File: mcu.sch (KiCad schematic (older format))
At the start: 17 parts, among them J3 debug+programing, J4 I2c oled, U4 STM32F103C8Tx, U5 SM353LT

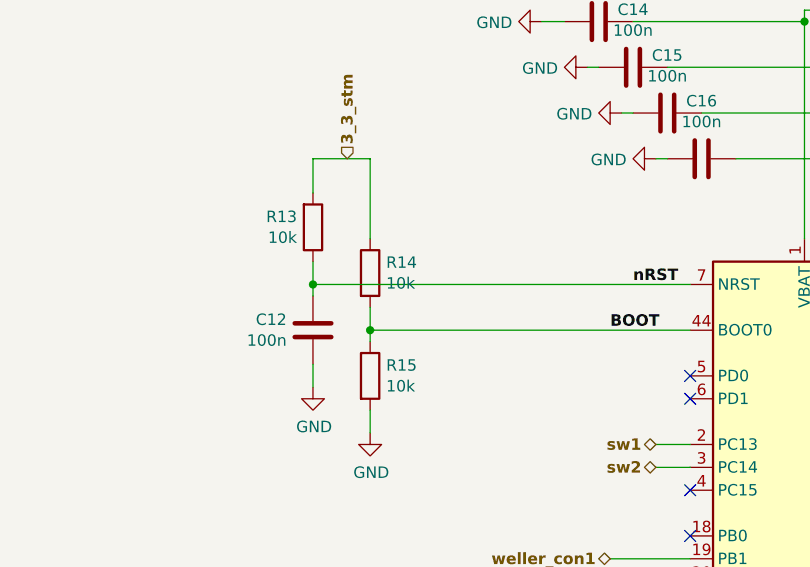
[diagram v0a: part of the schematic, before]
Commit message: update błędnego podpięcia pmosa na wejściu do układu, oras software testujący oled, przyciski i ledy
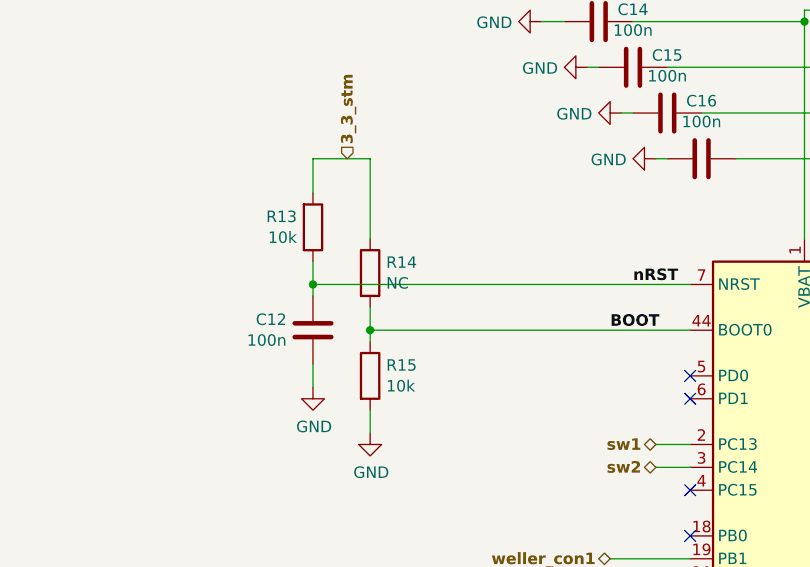
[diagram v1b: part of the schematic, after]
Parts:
- R14: value 10k -> NC
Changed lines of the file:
@@
 Wire Wire Line
 	6600 1200 6700 1200
-Text HLabel 4500 1850 1    50   Input ~ 6
+Text HLabel 4500 1850 1    50   Input ~ 10
 3_3_stm
-Text Label 6900 1600 0    50   ~ 6
+Text Label 6900 1600 0    50   ~ 10
 3_3v_analog
 $Comp
@@
 Wire Wire Line
 	4600 3050 4600 2950
-Text HLabel 6700 1050 1    50   Input ~ 6
+Text HLabel 6700 1050 1    50   Input ~ 10
 3_3_stm
 Wire Wire Line
@@
 Wire Wire Line
 	4350 1850 4350 2000
-Text HLabel 5850 3100 0    50   BiDi ~ 6
+Text HLabel 5850 3100 0    50   BiDi ~ 10
 sw1
-Text HLabel 5850 3200 0    50   BiDi ~ 6
+Text HLabel 5850 3200 0    50   BiDi ~ 10
 sw2
-Text HLabel 5750 3800 0    50   Output ~ 6
+Text HLabel 5750 3800 0    50   Output ~ 10
 led_g
-Text HLabel 5750 3900 0    50   Output ~ 6
+Text HLabel 5750 3900 0    50   Output ~ 10
 led_r
-Text HLabel 5750 4000 0    50   Output ~ 6
+Text HLabel 5750 4000 0    50   Output ~ 10
 led_y
-Text HLabel 5650 3600 0    50   BiDi ~ 6
+Text HLabel 5650 3600 0    50   BiDi ~ 10
 weller_con1
-Text HLabel 7650 4600 2    50   Output ~ 6
+Text HLabel 7650 4600 2    50   Output ~ 10
 PWM_heater
 Wire Wire Line
@@
 Wire Wire Line
 	7300 4900 7650 4900
-Text Label 7650 4800 0    50   ~ 6
+Text Label 7650 4800 0    50   ~ 10
 SWDIO
-Text Label 7650 4900 0    50   ~ 6
+Text Label 7650 4900 0    50   ~ 10
 SWCLK
-Text Label 5750 2400 0    50   ~ 6
+Text Label 5750 2400 0    50   ~ 10
 nRST
 Wire Wire Line
@@
 Wire Wire Line
 	6500 5500 6600 5500
-Text Label 1900 6850 0    50   ~ 6
+Text Label 1900 6850 0    50   ~ 10
 nRST
-Text Label 1900 6450 0    50   ~ 6
+Text Label 1900 6450 0    50   ~ 10
 SWDIO
-Text Label 1900 6550 0    50   ~ 6
+Text Label 1900 6550 0    50   ~ 10
 SWCLK
 Connection ~ 6900 1950
@@
 Wire Wire Line
 	6700 1650 6700 2200
-Text Label 5650 2600 0    50   ~ 6
+Text Label 5650 2600 0    50   ~ 10
 BOOT
 $Comp
@@
 Wire Wire Line
 	1550 3900 1100 3900
-Text HLabel 1100 3800 0    50   Input ~ 6
+Text HLabel 1100 3800 0    50   Input ~ 10
 3_3_stm
 Wire Wire Line
@@
 Wire Wire Line
 	1550 3600 1100 3600
-Text Label 1100 3600 0    50   ~ 6
+Text Label 1100 3600 0    50   ~ 10
 sda
-Text Label 1100 3700 0    50   ~ 6
+Text Label 1100 3700 0    50   ~ 10
 scl
-Text Label 5750 4200 0    50   ~ 6
+Text Label 5750 4200 0    50   ~ 10
 sda
 Wire Wire Line
 	5750 4200 6000 4200
-Text Label 5750 4100 0    50   ~ 6
+Text Label 5750 4100 0    50   ~ 10
 scl
 Wire Wire Line
@@
 Wire Wire Line
 	1300 3700 1100 3700
-Text HLabel 1150 3300 0    50   Input ~ 6
+Text HLabel 1150 3300 0    50   Input ~ 10
 3_3_stm
 Wire Wire Line
@@
 Wire Wire Line
 	7400 3800 7300 3800
-Text HLabel 7400 3800 2    50   Input ~ 6
+Text HLabel 7400 3800 2    50   Input ~ 10
 termocouple
 NoConn ~ 7300 3700
@@
 	-1   0    0    -1
 $EndComp
-Text Label 7650 3500 2    50   ~ 6
+Text Label 7650 3500 2    50   ~ 10
 hall_in
 Wire Wire Line
 	7300 3500 7650 3500
-Text Label 1150 5200 2    50   ~ 6
+Text Label 1150 5200 2    50   ~ 10
 hall_in
 $Comp
@@
 Wire Wire Line
 	1800 4900 1800 4850
-Text HLabel 1800 4800 1    50   Input ~ 6
+Text HLabel 1800 4800 1    50   Input ~ 10
 3_3_stm
 Wire Wire Line
 	1150 5200 1200 5200
-Text HLabel 1200 6450 0    50   Input ~ 6
+Text HLabel 1200 6450 0    50   Input ~ 10
 3_3_stm
 $Comp
@@
 Wire Wire Line
 	7300 4300 7650 4300
-Text Label 7650 4300 2    50   ~ 6
+Text Label 7650 4300 2    50   ~ 10
 usart_rx
-Text Label 7650 4400 2    50   ~ 6
+Text Label 7650 4400 2    50   ~ 10
 usart_tx
-Text Label 7650 4500 2    50   ~ 6
+Text Label 7650 4500 2    50   ~ 10
 usart_ck
 Wire Wire Line
@@
 Wire Wire Line
 	7300 4400 7650 4400
-Text Label 1200 6550 2    50   ~ 6
+Text Label 1200 6550 2    50   ~ 10
 usart_rx
-Text Label 1200 6650 2    50   ~ 6
+Text Label 1200 6650 2    50   ~ 10
 usart_tx
-Text Label 1200 6750 2    50   ~ 6
+Text Label 1200 6750 2    50   ~ 10
 usart_ck
 Wire Wire Line
@@
 Wire Wire Line
 	7400 3600 7300 3600
-Text HLabel 7400 3600 2    50   Input ~ 6
+Text HLabel 7400 3600 2    50   Input ~ 10
 input_sense
 NoConn ~ 7300 3900
@@
 P 4600 2350
 F 0 "R14" H 4670 2396 50  0000 L CNN
-F 1 "10k" H 4670 2305 50  0000 L CNN
+F 1 "NC" H 4670 2305 50  0000 L CNN
 F 2 "Resistor_SMD:R_0603_1608Metric" V 4530 2350 50  0001 C CNN
 F 3 "~" H 4600 2350 50  0001 C CNN
@@
 	1    0    0    -1
 $EndComp
-Text Notes 750  3150 0    50   ~ 6
+Text Notes 750  3150 0    50   ~ 10
 OLED 0,91' 4P 128x32 na I2C - SSD1306
-Text Notes 1250 2050 0    50   ~ 6
+Text Notes 1250 2050 0    50   ~ 10
 TEMP_SENSOR ?
-Text Notes 8400 3250 0    50   ~ 6
+Text Notes 8400 3250 0    50   ~ 10
 Wyprowadzenie pinów na test pointy ?
 Wire Notes Line
